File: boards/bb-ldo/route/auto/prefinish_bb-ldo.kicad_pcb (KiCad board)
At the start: 2 copper layers, 50 x 26.4 mm, 5 parts, among them J1 2P 5.08mm THT screw terminal, J2 2P 5.08mm THT screw terminal, U1 AMS1117-3.3

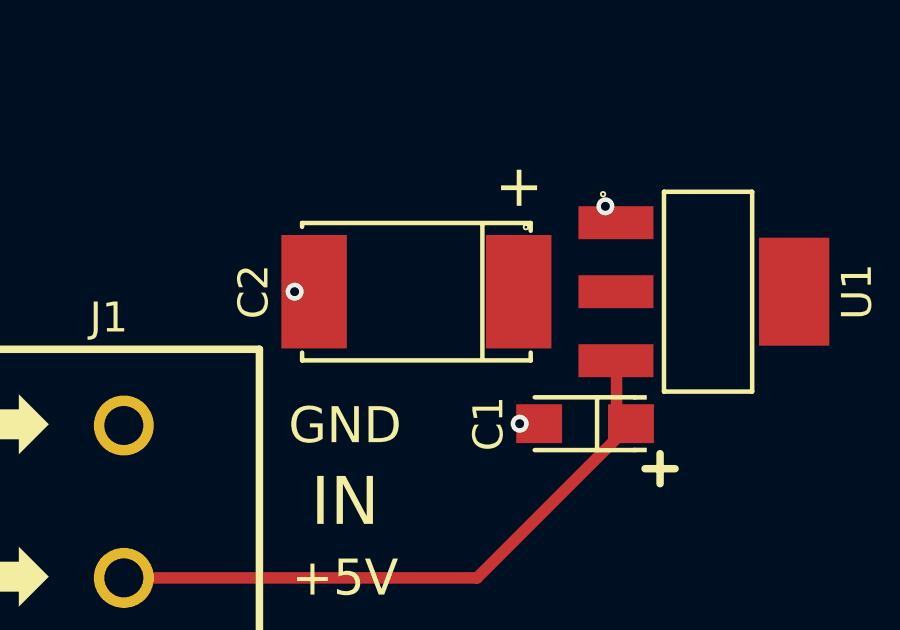
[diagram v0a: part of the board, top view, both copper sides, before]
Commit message: ai-ee bb-ldo: drc_routed pass (100% completion, pour 1199 mm2 one island)
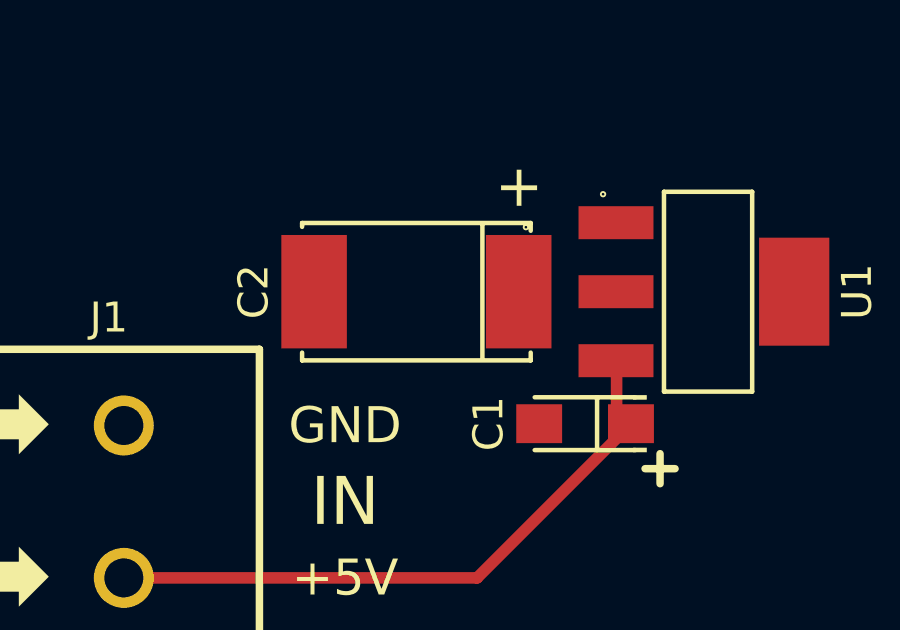
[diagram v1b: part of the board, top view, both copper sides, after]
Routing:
- net GND: vias 3 -> 0
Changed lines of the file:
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@@
 		)
-	)
-	(via
-		(at 17.318 32.91)
-		(size 0.6)
-		(drill 0.3)
-		(layers "F.Cu" "B.Cu")
-		(net "GND")
-	)
-	(via
-		(at 24.82 37.31)
-		(size 0.6)
-		(drill 0.3)
-		(layers "F.Cu" "B.Cu")
-		(net "GND")
-	)
-	(via
-		(at 27.677 30.064)
-		(size 0.6)
-		(drill 0.3)
-		(layers "F.Cu" "B.Cu")
-		(net "GND")
 	)
 	(segment
